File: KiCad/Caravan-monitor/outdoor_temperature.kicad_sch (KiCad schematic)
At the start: 3 parts, among them J3 Conn_01x02_Pin

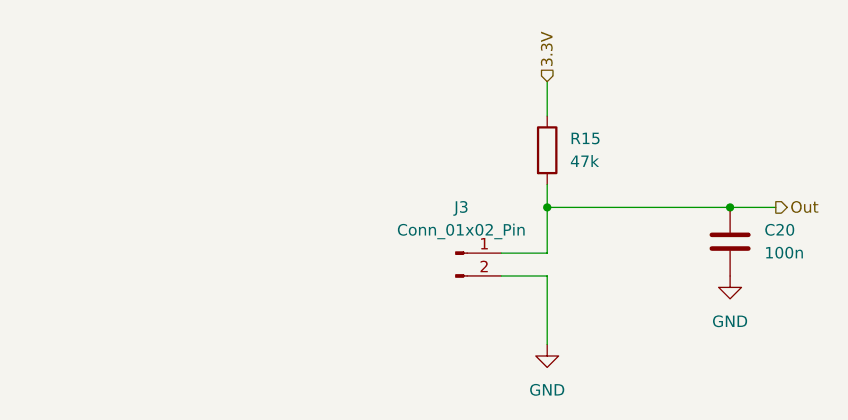
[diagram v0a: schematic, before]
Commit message: Display schematics
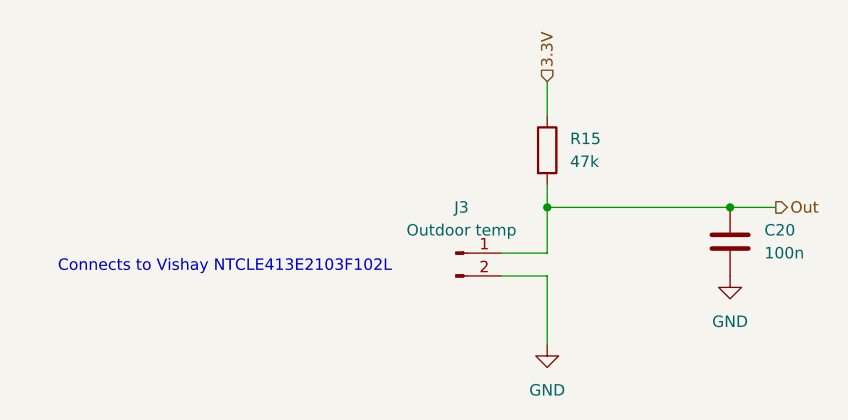
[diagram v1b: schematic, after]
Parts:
- J3: value Conn_01x02_Pin -> Outdoor temp
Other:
- note added: "Connects to Vishay NTCLE413E2103F102L"
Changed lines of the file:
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@@
 	(generator_version "9.0")
 	(paper "A4")
+	(text "Connects to Vishay NTCLE413E2103F102L"
+		(exclude_from_sim no)
+		(at 96.266 92.964 0)
+		(effects
+			(font
+				(size 1.27 1.27)
+			)
+		)
+	)
 	(junction
 		(at 132.08 86.36)
@@
 			)
 		)
-		(property "Value" "Conn_01x02_Pin"
+		(property "Value" "Outdoor temp"
 			(at 122.555 88.9 0)
 			(effects

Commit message: Schematics done
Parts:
- C20: footprint Capacitor_SMD:C_0805_2012Metric_Pad1.18x1.45mm_HandSolder -> Capacitor_SMD:C_0402_1005Metric_Pad0.74x0.62mm_HandSolder
- R15: footprint Resistor_SMD:R_0805_2012Metric_Pad1.20x1.40mm_HandSolder -> Resistor_SMD:R_0402_1005Metric_Pad0.72x0.64mm_HandSolder
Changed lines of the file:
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@@
 			)
 		)
-		(property "Footprint" "Capacitor_SMD:C_0805_2012Metric_Pad1.18x1.45mm_HandSolder"
+		(property "Footprint" "Capacitor_SMD:C_0402_1005Metric_Pad0.74x0.62mm_HandSolder"
 			(at 153.3652 93.98 0)
 			(effects
@@
 			)
 		)
-		(property "Footprint" "Resistor_SMD:R_0805_2012Metric_Pad1.20x1.40mm_HandSolder"
+		(property "Footprint" "Resistor_SMD:R_0402_1005Metric_Pad0.72x0.64mm_HandSolder"
 			(at 130.302 80.01 90)
 			(effects

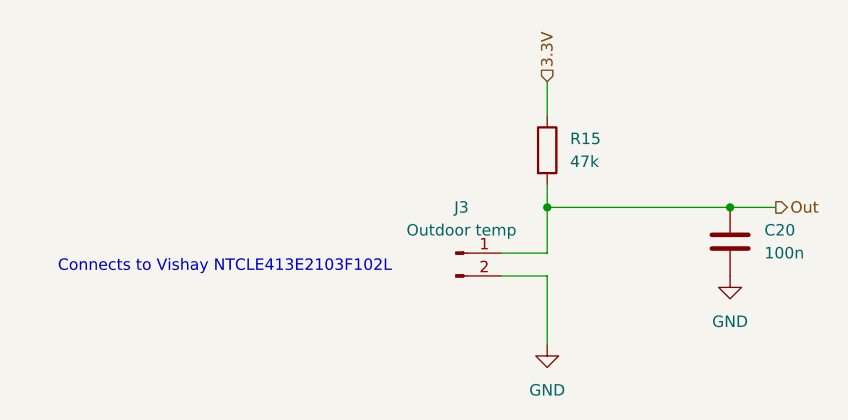
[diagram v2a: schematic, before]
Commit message: Schematic updates
Parts changed for JLCPCB assembly compatibility
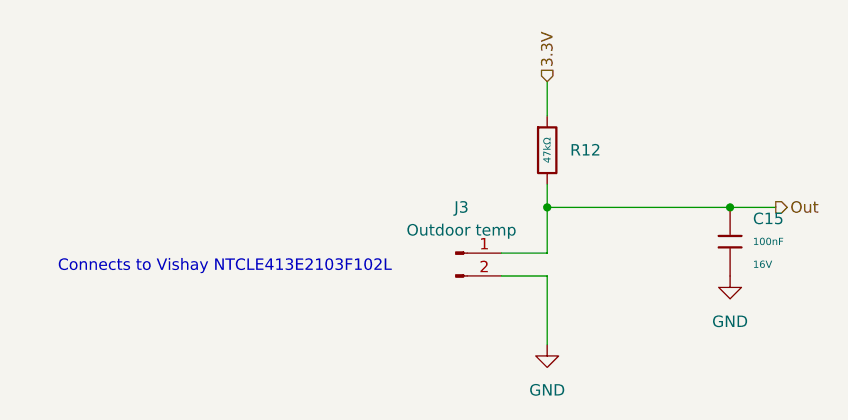
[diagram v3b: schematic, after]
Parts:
- removed C20: 100n, Capacitor_SMD:C_0402_1005Metric_Pad0.74x0.62mm_HandSolder, symbol Device:C
- removed R15: 47k, Resistor_SMD:R_0402_1005Metric_Pad0.72x0.64mm_HandSolder, symbol Device:R
- added C15: 100nF, PCM_JLCPCB:C_0402, symbol PCM_JLCPCB-Capacitors:0402,100nF
- added R12: 47kΩ, PCM_JLCPCB:R_0402, symbol PCM_JLCPCB-Resistors:0402,47kΩ
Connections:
- net 3.3V: now also R12.1
- net GND: now also C15.2
- net Out: now also C15.1, R12.2
